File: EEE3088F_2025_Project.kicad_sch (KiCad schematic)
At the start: 40 parts, among them J1 Conn_02x16_Odd_Even, J2 USB_C_Receptacle_PowerOnly_6P, J3 Conn_01x02, Q1 PNP, SW1 SW_SPST, U1 HR8833, U2 HR8833, U3 TP4057, U4 HT7533-1, U5 TPS613222ADBV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

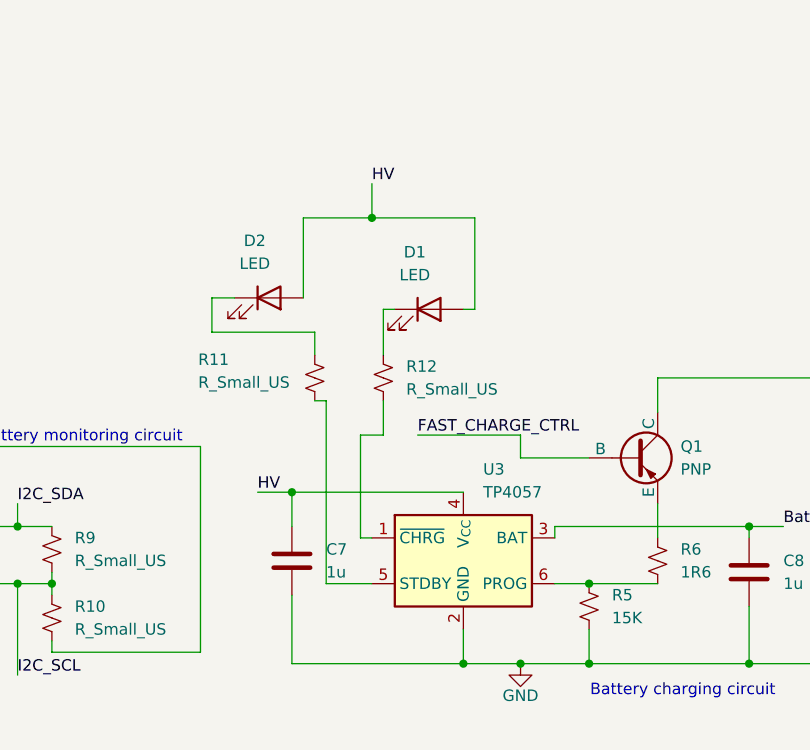
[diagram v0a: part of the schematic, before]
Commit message: Change charging IC to have 5 pins
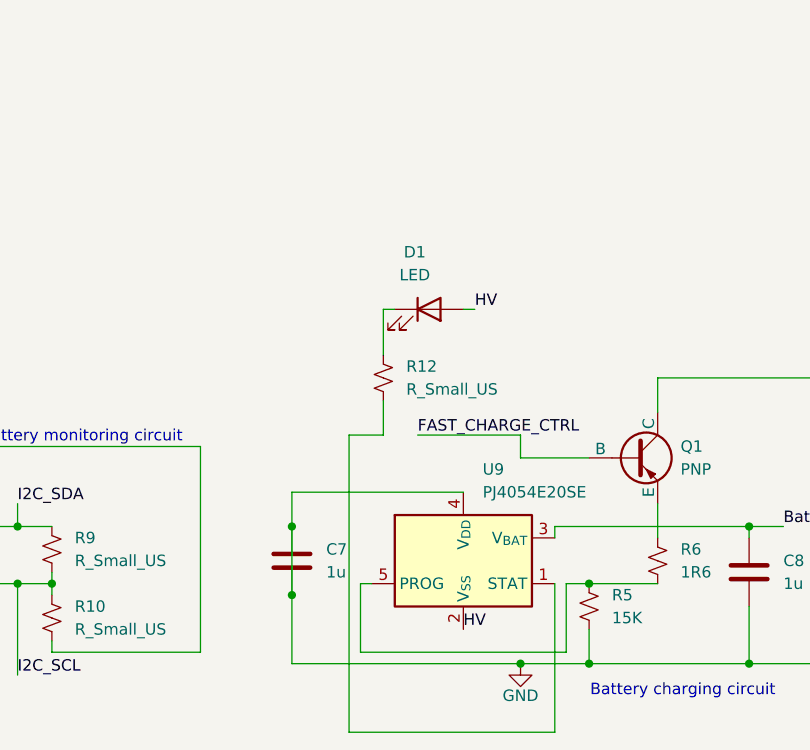
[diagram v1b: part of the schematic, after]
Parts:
- removed D2: LED, symbol Device:LED
- removed R11: R_Small_US, symbol Device:R_Small_US
- removed U3: TP4057, Package_TO_SOT_SMD:TSOT-23-6, symbol Battery_Management:TP4057
- added U9: PJ4054E20SE, Package_TO_SOT_SMD:SOT-23-5, symbol Battery_Management:MCP73831-2-OT
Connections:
- net Battery: now also U9.3 (V_{BAT})
- net GND: now also C7.1, U9.4 (V_{DD})
- net HV: now also U9.2 (V_{SS}); no longer C7.1
- net at R5.1, R6.2: now also U9.5 (PROG)
- net at R12.2: now also U9.1 (STAT)

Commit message: fix
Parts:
- added U3: MIC2026-1xM, Package_SO:SOIC-8_3.9x4.9mm_P1.27mm, symbol Power_Management:MIC2026-1xM
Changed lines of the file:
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@@
+	)
+	(symbol
+		(lib_id "Power_Management:MIC2026-1xM")
+		(at 78.74 95.25 0)
+		(unit 1)
+		(exclude_from_sim no)
+		(in_bom yes)
+		(on_board yes)
+		(dnp no)
+		(fields_autoplaced yes)
+		(property "Reference" "U3"
+			(at 78.74 80.01 0)
+			(effects
+				(font
+					(size 1.27 1.27)
+				)
+			)
+		)
+		(property "Value" "MIC2026-1xM"
+			(at 78.74 82.55 0)
+			(effects
+				(font
+					(size 1.27 1.27)
+				)
+			)
+		)
+		(property "Footprint" "Package_SO:SOIC-8_3.9x4.9mm_P1.27mm"
+			(at 78.74 95.25 0)
+			(effects
+				(font
+					(size 1.27 1.27)
+				)
+				(hide yes)
+			)
+		)
+		(property "Datasheet" "https://ww1.microchip.com/downloads/aemDocuments/documents/APID/ProductDocuments/DataSheets/MIC2026-MIC2076-Dual-Channel-Power-Distribution-Switch-DS20006443A.pdf"
+			(at 78.74 95.25 0)
+			(effects
+				(font
+					(size 1.27 1.27)
+				)
+				(hide yes)
+			)
+		)
+		(property "Description" "Dual-channel, high side, power distribution switch, 2.7V-5.5V, Active High Output, SOIC-8"
+			(at 78.74 95.25 0)
+			(effects
+				(font
+					(size 1.27 1.27)
+				)
+				(hide yes)
+			)
+		)
+		(pin "8"
+		)
+		(pin "4"
+		)
+		(pin "1"
+		)
+		(pin "7"
+		)
+		(pin "2"
+		)
+		(pin "3"
+		)
+		(pin "6"
+		)
+		(pin "5"
+		)
+		(instances
+			(project ""
+				(path "/0c96e665-4374-49a7-9a3f-3cff1e0343ef"
+					(reference "U3")
+					(unit 1)
+				)
+			)
+		)
 	)
 	(symbol

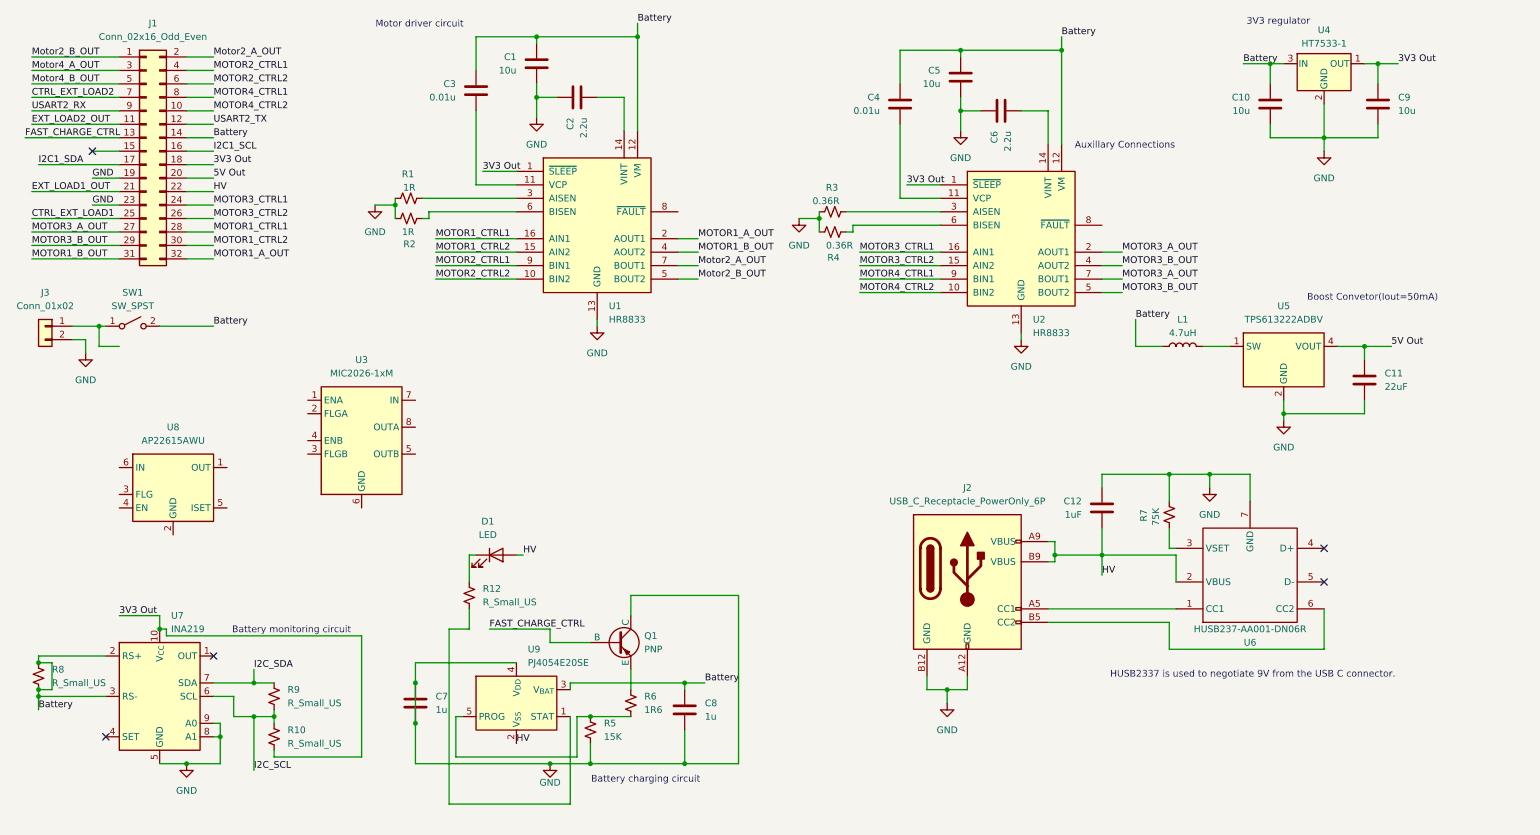
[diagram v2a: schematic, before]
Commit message: Added footprints and LCSC numbers
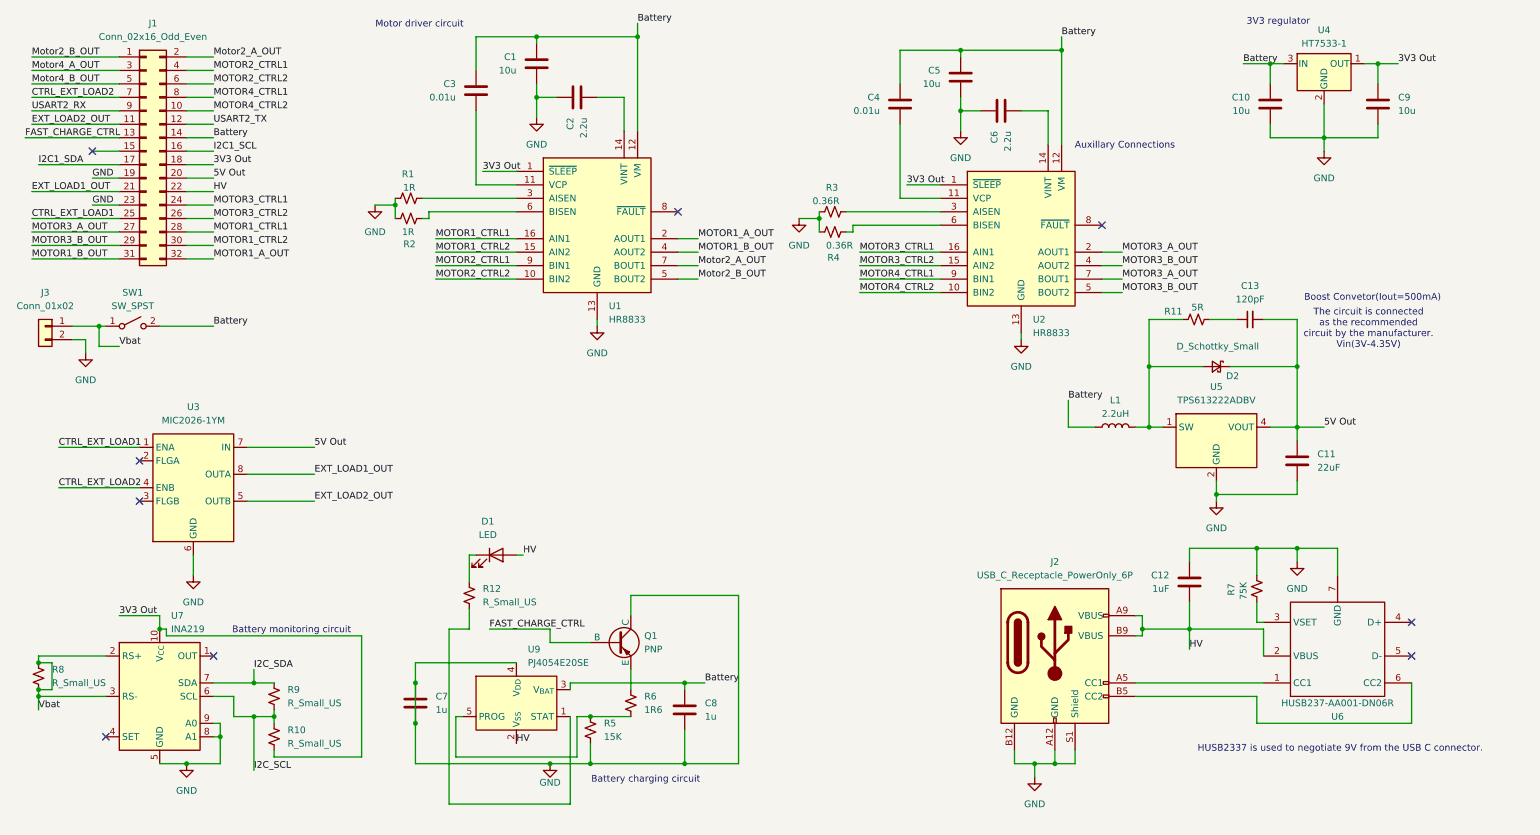
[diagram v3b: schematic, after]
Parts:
- removed U8: AP22615AWU, Package_TO_SOT_SMD:SOT-23-6, symbol Regulator_Linear:AP22615AWU
- added C13: 120pF, Capacitor_SMD:C_0201_0603Metric_Pad0.64x0.40mm_HandSolder, symbol Device:C_Small
- added D2: D_Schottky_Small, Diode_SMD:D_SMA, symbol Device:D_Schottky_Small
- added R11: 5R, Resistor_SMD:R_1206_3216Metric_Pad1.30x1.75mm_HandSolder, symbol Device:R_Small_US
- C1, C10, C11, C12, C2, C3, C4, C5, C6, C7, C8, C9: footprint (none) -> Capacitor_SMD:C_0201_0603Metric
- D1, R1, R10, R12, R2, R3, R4, R5, R6, R7, R8, R9: footprint (none) -> Resistor_SMD:R_0201_0603Metric_Pad0.64x0.40mm_HandSolder
- J1: footprint (none) -> Connector_PinHeader_2.54mm:PinHeader_2x16_P2.54mm_Vertical
- J3: footprint (none) -> Connector_PinHeader_2.54mm:PinHeader_1x02_P2.54mm_Vertical; LCSC (none) -> C541760
- L1: value 4.7uH -> 2.2uH; footprint (none) -> Inductor_SMD:L_1008_2520Metric_Pad1.43x2.20mm_HandSolder; LCSC (none) -> C86092
- Q1: footprint (none) -> Transistor_Power:GaN_Systems_GaNPX-3_5x6.6mm_Drain2.93x0.6mm
- SW1: footprint (none) -> Button_Switch_THT:SW_Tactile_SPST_Angled_PTS645Vx83-2LFS; LCSC (none) -> C2887259
- U1, U2: footprint Package_SO:TSSOP-16-1EP_4.4x5mm_P0.65mm_EP3x3mm -> Package_SO:TSSOP-16_4.4x5mm_P0.65mm
- U3: value MIC2026-1xM -> MIC2026-1YM
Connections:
- net 5V Out: now also U3.7 (IN), C13.2, D2.1 (K)
- net Battery: no longer R8.1, R8.2, U7.2 (RS+), U7.3 (RS-)
- net CTRL_EXT_LOAD1: now also U3.1 (ENA)
- net CTRL_EXT_LOAD2: now also U3.4 (ENB)
- net EXT_LOAD1_OUT: now also U3.8 (OUTA)
- net EXT_LOAD2_OUT: now also U3.5 (OUTB)
- net GND: now also J2.S1 (Shield), U3.6 (GND)
- net at L1.2, U5.1 (SW): now also D2.2 (A), R11.1
- net Vbat: now reaches J3.1 (Pin_1), SW1.1 (A)
- net Vbat: now also R8.1, R8.2, U7.2 (RS+), U7.3 (RS-)
- new net: C13.1, R11.2
- no-connect marks 5 -> 9
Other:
- note added: "Boost Convetor(Iout=500mA)"
- note added: "The circuit is connected as the recommended circuit by the manufacturer. Vin(3V-4.35V)"
- note removed: "Boost Convetor(Iout=50mA)"
- moved on the sheet: C11, C12, L1, R7, U3, U5, U6

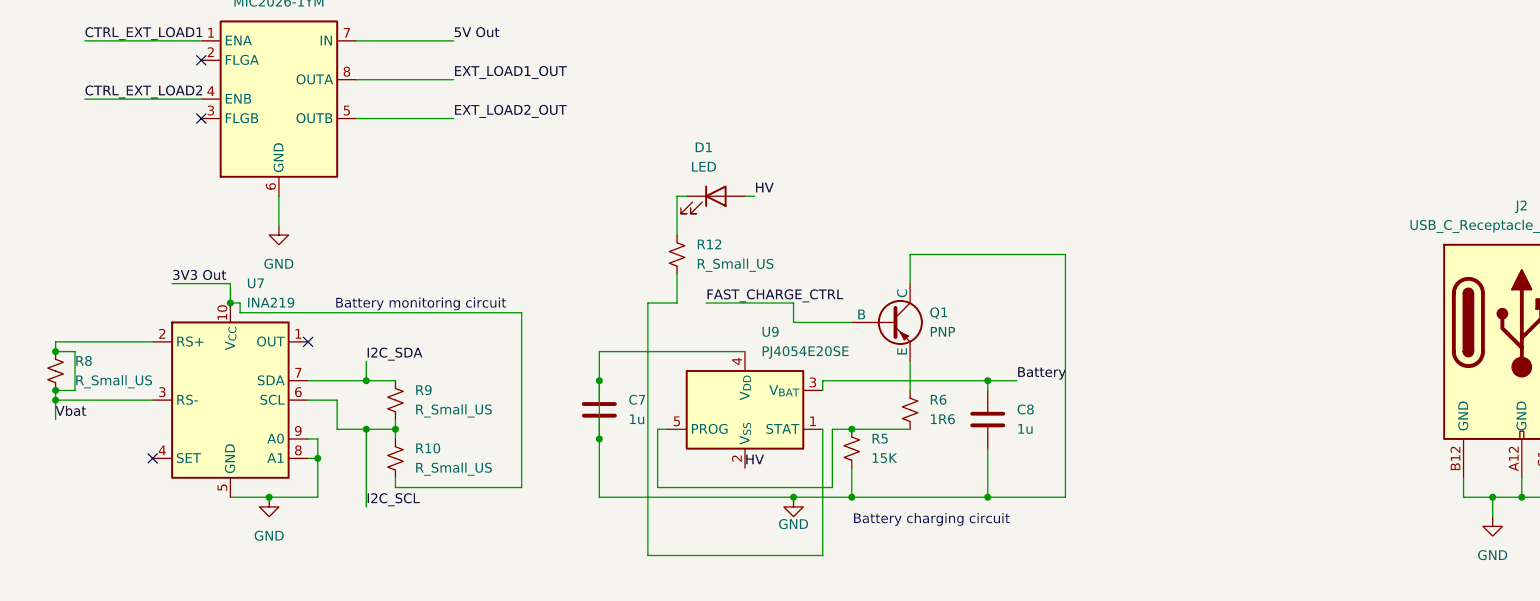
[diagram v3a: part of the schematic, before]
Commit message: Changed charging IC
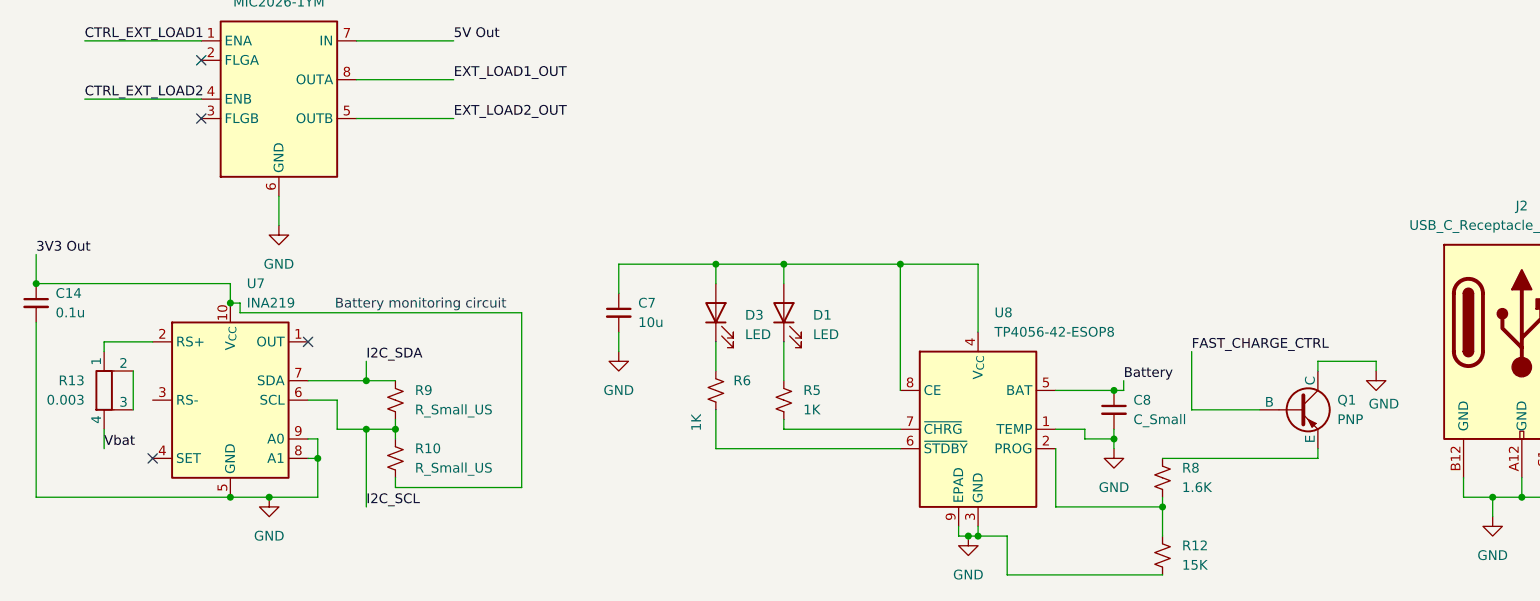
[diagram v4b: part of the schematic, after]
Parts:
- removed C7, C8: 1u, Capacitor_SMD:C_0201_0603Metric, symbol Device:C
- removed U9: PJ4054E20SE, Package_TO_SOT_SMD:SOT-23-5, symbol Battery_Management:MCP73831-2-OT
- added C14: 0.1u, symbol Device:C_Small
- added C7: 10u, Capacitor_SMD:C_0201_0603Metric_Pad0.64x0.40mm_HandSolder, symbol Device:C_Small
- added C8: C_Small, symbol Device:C_Small
- added D3: LED, LED_SMD:LED_0201_0603Metric_Pad0.64x0.40mm_HandSolder, symbol Device:LED
- added R13: 0.003, Resistor_SMD:R_Shunt_Vishay_WSK2512_6332Metric_T1.19mm, symbol Device:R_Shunt
- added U8: TP4056-42-ESOP8, Package_SO:SOIC-8-1EP_3.9x4.9mm_P1.27mm_EP2.41x3.3mm_ThermalVias, symbol Battery_Management:TP4056-42-ESOP8
- D1: footprint Resistor_SMD:R_0201_0603Metric_Pad0.64x0.40mm_HandSolder -> LED_SMD:LED_0201_0603Metric_Pad0.64x0.40mm_HandSolder
- Q1: footprint Transistor_Power:GaN_Systems_GaNPX-3_5x6.6mm_Drain2.93x0.6mm -> (none)
- R12: value R_Small_US -> 15K
- R5: value 15K -> 1K
- R6: value 1R6 -> 1K
- R8: value R_Small_US -> 1.6K
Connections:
- net 3V3 Out: now also C14.1
- net Battery: now also C8.1, U8.5 (BAT)
- net GND: now also R12.2, C14.2, C7.2, C8.2, U8.1 (TEMP), U8.3 (GND), U8.9 (EPAD); no longer R5.2
- net HV: no longer D1.2 (A)
- net Vbat: now also R13.4; no longer R8.1, R8.2, U7.2 (RS+), U7.3 (RS-)
- net at R5.1: now also D1.1 (K); no longer R6.2
- net at R12.1: now also R8.2, U8.2 (PROG); no longer D1.1 (K)
- net at Q1.3 (E): now also R8.1; no longer R6.1
- new net: R13.1, U7.2 (RS+)
- new net: C7.1, D1.2 (A), D3.2 (A), U8.4 (V_{CC}), U8.8 (CE)
- new net: D3.1 (K), R6.1
- new net: R6.2, U8.6 (~{STDBY})
- new net: R5.2, U8.7 (~{CHRG})
- new net: R13.2, R13.3
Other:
- note removed: "Battery charging circuit"
